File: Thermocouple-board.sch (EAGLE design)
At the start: 91 parts, among them J1 RJ45, J10 1X2-3.5MM, J11 1X2-3.5MM, J12 1X2-3.5MM, J13 1X2-3.5MM, J2 RJ45, J3 1981584-1, J4 2.1MMJACKTHM, J5 ST-LINK, J6 HEADER-1X3, J7 UART, SW1 PUSHBUTTON, SW2 PUSHBUTTON, U1 STM32F042K6, U10 MAX31855, U11 MAX31855, U12 MAX31855, U13 MAX31855, U20 EEPROM-I2C, U21 EEPROM-I2C, U30 ST3485, U31 ST3485, U40 LP298XS, U70 TPS25921, Y1 8MHz

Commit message: Extended PCB length to 3.9 in
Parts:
- J4: device adafruit:2.1MMJACKTHM -> Thermocouple-board:2.1MMJACKTHM
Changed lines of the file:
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@@
 <part name="GND34" library="supply1" deviceset="GND" device=""/>
 <part name="GND35" library="supply1" deviceset="GND" device=""/>
-<part name="J4" library="adafruit" library_urn="urn:adsk.eagle:library:420" deviceset="2.1MMJACK" device="THM" package3d_urn="urn:adsk.eagle:package:6240341/1"/>
+<part name="J4" library="Thermocouple-board" deviceset="2.1MMJACK" device="THM"/>
 <part name="GND36" library="supply1" deviceset="GND" device=""/>
 <part name="D3" library="SparkFun-DiscreteSemi" library_urn="urn:adsk.eagle:library:514" deviceset="DIODE-SCHOTTKY" device="-B340A" package3d_urn="urn:adsk.eagle:package:38443/1" value="3A/40V/500mV"/>

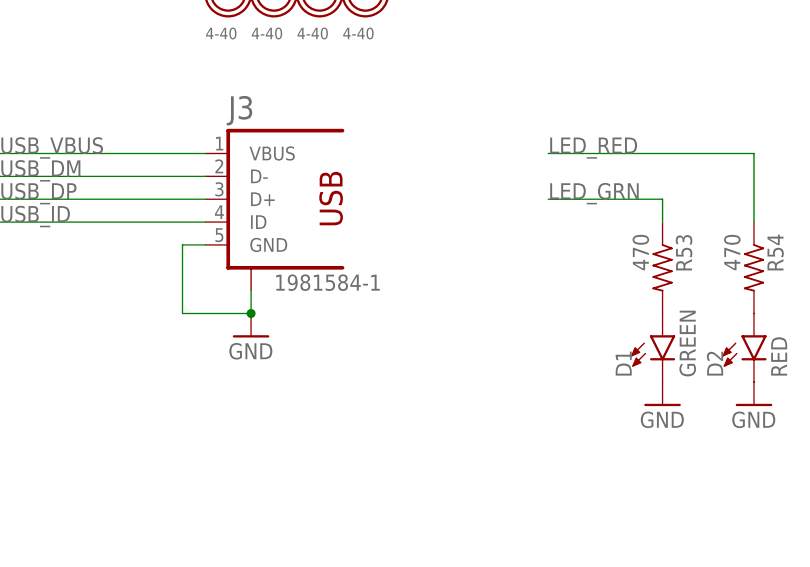
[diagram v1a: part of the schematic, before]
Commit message: Updated micro USB conn to long pads
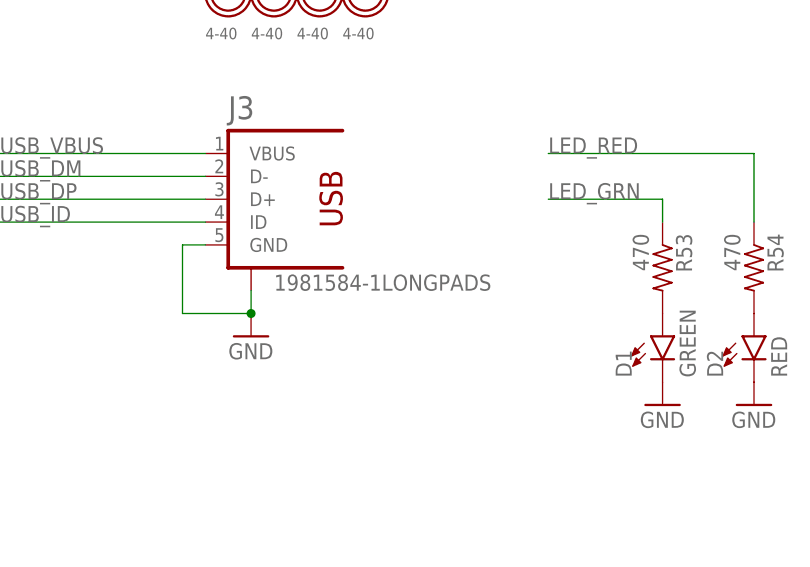
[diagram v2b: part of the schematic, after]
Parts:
- J3: value 1981584-1 -> 1981584-1LONGPADS; device audio amplifier example:1981584-1 -> Thermocouple-board:1981584-1LONGPADS
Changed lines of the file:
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@@
 <part name="+3V20" library="supply1" deviceset="+3V3" device=""/>
 <part name="+3V22" library="supply1" deviceset="+3V3" device=""/>
-<part name="J3" library="audio amplifier example" library_urn="urn:adsk.eagle:library:970892" deviceset="1981584-1" device="" package3d_urn="urn:adsk.eagle:package:970926/2"/>
+<part name="J3" library="Thermocouple-board" deviceset="1981584-1" device="LONGPADS"/>
 <part name="GND24" library="supply1" deviceset="GND" device=""/>
 <part name="C40" library="adafruit" deviceset="C-US" device="C0805K" value="1uF"/>

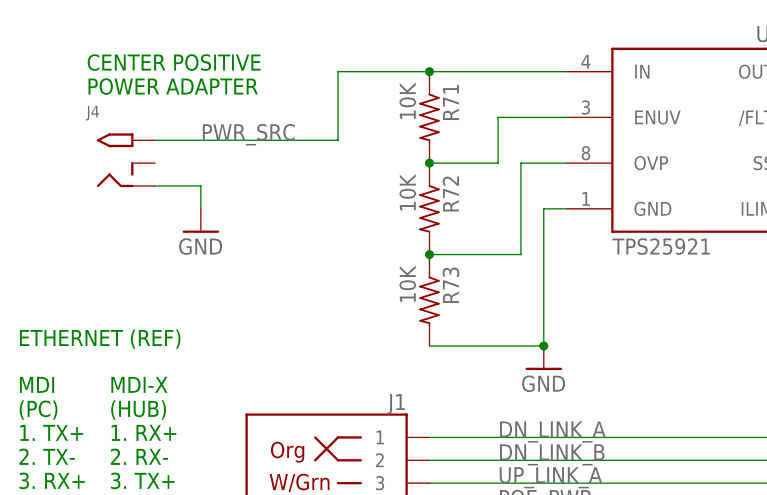
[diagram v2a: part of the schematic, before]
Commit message: Mostly routed. Needs connector alignment and hold downs.
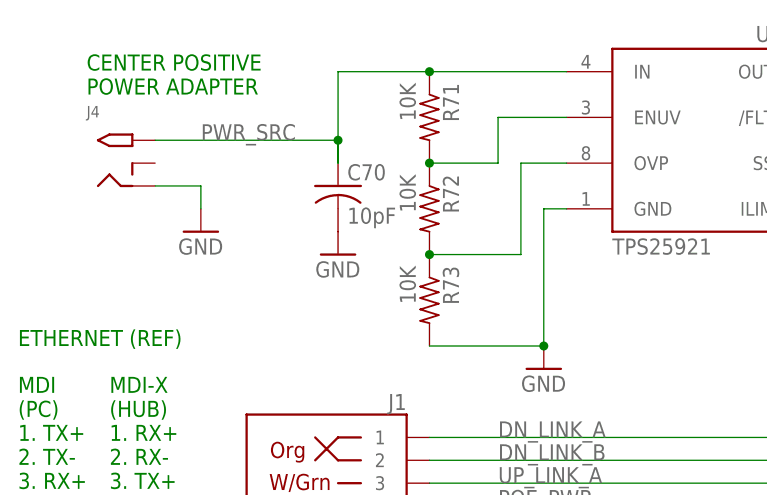
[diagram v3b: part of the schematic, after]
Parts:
- added C70: 10pF, adafruit:C-USC0805K
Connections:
- net GND: now also C70.2
- net PWR_SRC: now also C70.1
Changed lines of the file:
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@@
 <part name="R40" library="adafruit" deviceset="R-US_" device="R0805" value="120"/>
 <part name="R41" library="adafruit" deviceset="R-US_" device="R0805" value="120"/>
+<part name="C70" library="adafruit" library_urn="urn:adsk.eagle:library:420" deviceset="C-US" device="C0805K" package3d_urn="urn:adsk.eagle:package:6240397/1" value="10pF"/>
+<part name="GND40" library="supply1" deviceset="GND" device=""/>
 </parts>
 <sheets>
@@
 <attribute name="VALUE" x="296.418" y="-34.29" size="1.778" layer="96" rot="R270"/>
 </instance>
+<instance part="C70" gate="G$1" x="-12.7" y="121.92" smashed="yes">
+<attribute name="NAME" x="-11.684" y="122.555" size="1.778" layer="95"/>
+<attribute name="VALUE" x="-11.684" y="117.729" size="1.778" layer="96"/>
+</instance>
+<instance part="GND40" gate="1" x="-12.7" y="114.3" smashed="yes">
+<attribute name="VALUE" x="-15.24" y="111.76" size="1.778" layer="96"/>
+</instance>
 </instances>
 <busses>
@@
 <wire x1="60.96" y1="121.92" x2="60.96" y2="124.46" width="0.1524" layer="91"/>
 </segment>
+<segment>
+<pinref part="C70" gate="G$1" pin="2"/>
+<pinref part="GND40" gate="1" pin="GND"/>
+</segment>
 </net>
 <net name="SPI_CS0_N" class="0">
@@
 <pinref part="U70" gate="G$1" pin="IN"/>
 <wire x1="-33.02" y1="127" x2="-12.7" y2="127" width="0.1524" layer="91"/>
+<wire x1="-12.7" y1="127" x2="-12.7" y2="124.46" width="0.1524" layer="91"/>
+<wire x1="-12.7" y1="124.46" x2="-12.7" y2="127" width="0.1524" layer="91"/>
 <wire x1="-12.7" y1="127" x2="-12.7" y2="134.62" width="0.1524" layer="91"/>
 <wire x1="-12.7" y1="134.62" x2="-2.54" y2="134.62" width="0.1524" layer="91"/>
@@
 <junction x="-2.54" y="134.62"/>
 <label x="-27.94" y="127" size="1.778" layer="95"/>
-</segment>
-</net>
+<pinref part="C70" gate="G$1" pin="1"/>
+<junction x="-12.7" y="127"/>
+</segment>
+</net>

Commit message: Routing complete
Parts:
- added MH10, MH11, MH12, MH13, MH14, MH15, MH16, MH5, MH6, MH7, MH8, MH9: HOLD_DOWN, Thermocouple-board:HOLD_DOWN
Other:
- moved on the sheet: C10, C11, C12, C13, C14, C15, C16, C17, FB1, FB2, FB3, FB4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

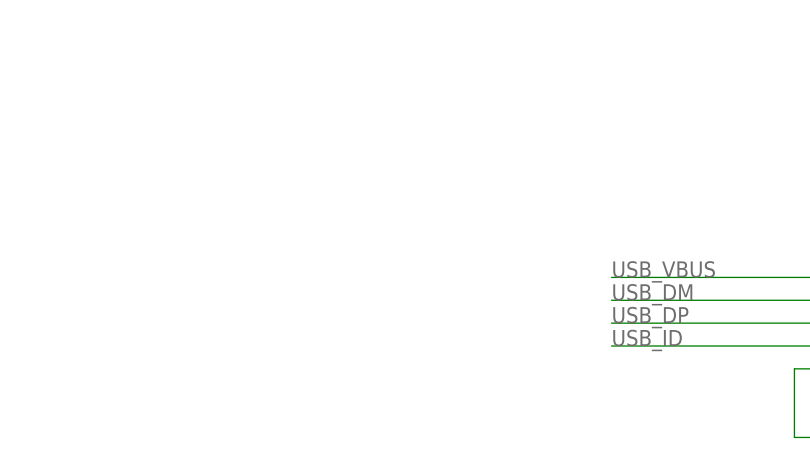
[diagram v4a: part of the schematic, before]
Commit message: Added ground TPs
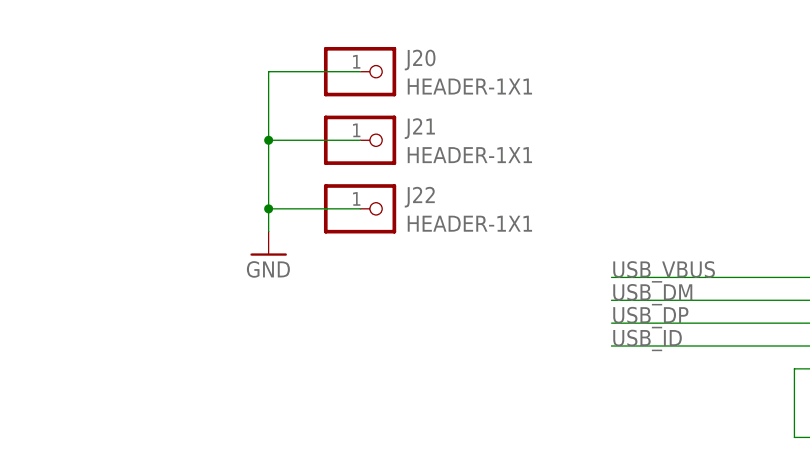
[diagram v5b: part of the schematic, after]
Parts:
- added J20, J21, J22: HEADER-1X1, Thermocouple-board:HEADER-1X1
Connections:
- net GND: now also J20.1, J21.1, J22.1
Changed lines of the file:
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@@
 <part name="MH15" library="Thermocouple-board" deviceset="HOLD_DOWN" device=""/>
 <part name="MH16" library="Thermocouple-board" deviceset="HOLD_DOWN" device=""/>
+<part name="J20" library="Thermocouple-board" deviceset="HEADER-1X1" device=""/>
+<part name="J21" library="Thermocouple-board" deviceset="HEADER-1X1" device=""/>
+<part name="J22" library="Thermocouple-board" deviceset="HEADER-1X1" device=""/>
+<part name="GND41" library="supply1" deviceset="GND" device=""/>
 </parts>
 <sheets>
@@
 <attribute name="NAME" x="-50.8" y="-82.55" size="1.27" layer="95" rot="R90"/>
 </instance>
+<instance part="J20" gate="G$1" x="142.24" y="134.62" smashed="yes">
+<attribute name="NAME" x="144.78" y="135.255" size="1.778" layer="95"/>
+<attribute name="VALUE" x="144.78" y="132.08" size="1.778" layer="96"/>
+</instance>
+<instance part="J21" gate="G$1" x="142.24" y="127" smashed="yes">
+<attribute name="NAME" x="144.78" y="127.635" size="1.778" layer="95"/>
+<attribute name="VALUE" x="144.78" y="124.46" size="1.778" layer="96"/>
+</instance>
+<instance part="J22" gate="G$1" x="142.24" y="119.38" smashed="yes">
+<attribute name="NAME" x="144.78" y="120.015" size="1.778" layer="95"/>
+<attribute name="VALUE" x="144.78" y="116.84" size="1.778" layer="96"/>
+</instance>
+<instance part="GND41" gate="1" x="129.54" y="114.3" smashed="yes">
+<attribute name="VALUE" x="127" y="111.76" size="1.778" layer="96"/>
+</instance>
 </instances>
 <busses>
@@
 <pinref part="GND40" gate="1" pin="GND"/>
 </segment>
+<segment>
+<pinref part="J22" gate="G$1" pin="1"/>
+<pinref part="GND41" gate="1" pin="GND"/>
+<wire x1="139.7" y1="119.38" x2="129.54" y2="119.38" width="0.1524" layer="91"/>
+<wire x1="129.54" y1="119.38" x2="129.54" y2="116.84" width="0.1524" layer="91"/>
+<junction x="129.54" y="119.38"/>
+<pinref part="J21" gate="G$1" pin="1"/>
+<wire x1="139.7" y1="127" x2="129.54" y2="127" width="0.1524" layer="91"/>
+<wire x1="129.54" y1="127" x2="129.54" y2="119.38" width="0.1524" layer="91"/>
+<pinref part="J20" gate="G$1" pin="1"/>
+<wire x1="139.7" y1="134.62" x2="129.54" y2="134.62" width="0.1524" layer="91"/>
+<wire x1="129.54" y1="134.62" x2="129.54" y2="127" width="0.1524" layer="91"/>
+<junction x="129.54" y="127"/>
+</segment>
 </net>

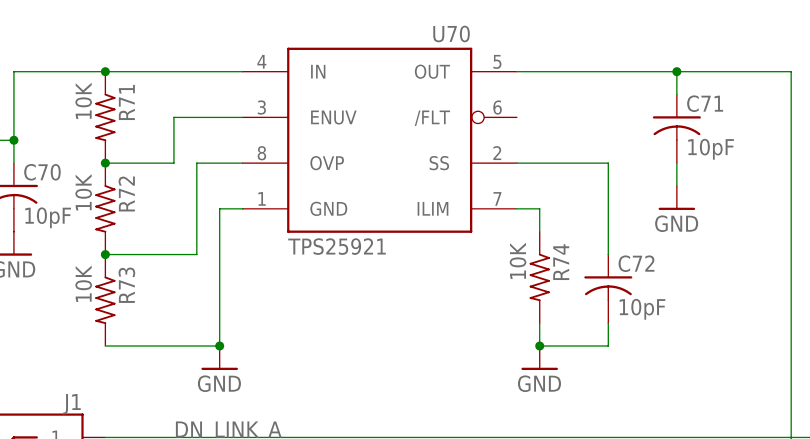
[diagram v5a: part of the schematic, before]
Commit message: Reroute efuse
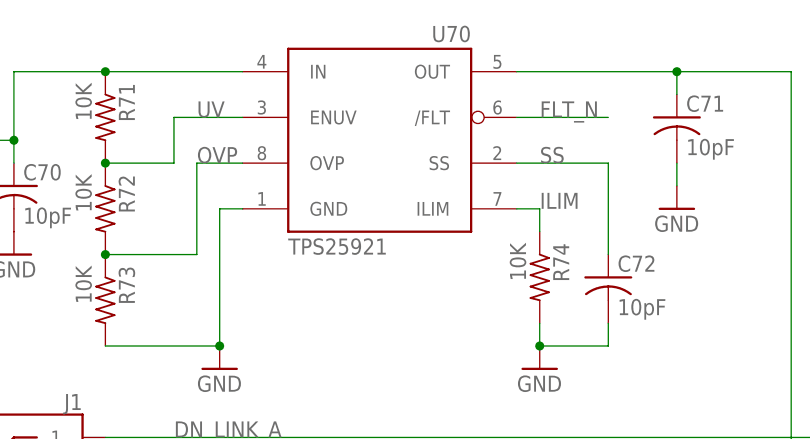
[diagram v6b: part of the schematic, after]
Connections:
- net N$23 renamed UV
- net N$24 renamed OVP
- net N$27 renamed ILIM
- net N$28 renamed SS
- new net FLT_N: U70./FLT
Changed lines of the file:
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@@
 </segment>
 </net>
-<net name="N$23" class="0">
+<net name="UV" class="0">
 <segment>
 <pinref part="R71" gate="G$1" pin="2"/>
@@
 <wire x1="5.08" y1="124.46" x2="5.08" y2="129.54" width="0.1524" layer="91"/>
 <wire x1="5.08" y1="129.54" x2="12.7" y2="129.54" width="0.1524" layer="91"/>
+<label x="7.62" y="129.54" size="1.778" layer="95"/>
 </segment>
 </net>
-<net name="N$24" class="0">
+<net name="OVP" class="0">
 <segment>
 <pinref part="R72" gate="G$1" pin="2"/>
@@
 <wire x1="7.62" y1="114.3" x2="7.62" y2="124.46" width="0.1524" layer="91"/>
 <wire x1="7.62" y1="124.46" x2="12.7" y2="124.46" width="0.1524" layer="91"/>
+<label x="7.62" y="124.46" size="1.778" layer="95"/>
 </segment>
 </net>
-<net name="N$27" class="0">
+<net name="ILIM" class="0">
 <segment>
 <pinref part="U70" gate="G$1" pin="ILIM"/>
@@
 <pinref part="R74" gate="G$1" pin="1"/>
 <wire x1="45.72" y1="119.38" x2="45.72" y2="116.84" width="0.1524" layer="91"/>
+<label x="45.72" y="119.38" size="1.778" layer="95"/>
 </segment>
 </net>
-<net name="N$28" class="0">
+<net name="SS" class="0">
 <segment>
 <pinref part="U70" gate="G$1" pin="SS"/>
@@
 <pinref part="C72" gate="G$1" pin="1"/>
 <wire x1="53.34" y1="124.46" x2="53.34" y2="114.3" width="0.1524" layer="91"/>
+<label x="45.72" y="124.46" size="1.778" layer="95"/>
 </segment>
 </net>
@@
 </segment>
 </net>
+<net name="FLT_N" class="0">
+<segment>
+<pinref part="U70" gate="G$1" pin="/FLT"/>
+<wire x1="43.18" y1="129.54" x2="53.34" y2="129.54" width="0.1524" layer="91"/>
+<label x="45.72" y="129.54" size="1.778" layer="95"/>
+</segment>
+</net>
